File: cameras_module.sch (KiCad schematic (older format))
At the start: 22 parts, among them J3 WE_68715014522, U4 PCA9547BS

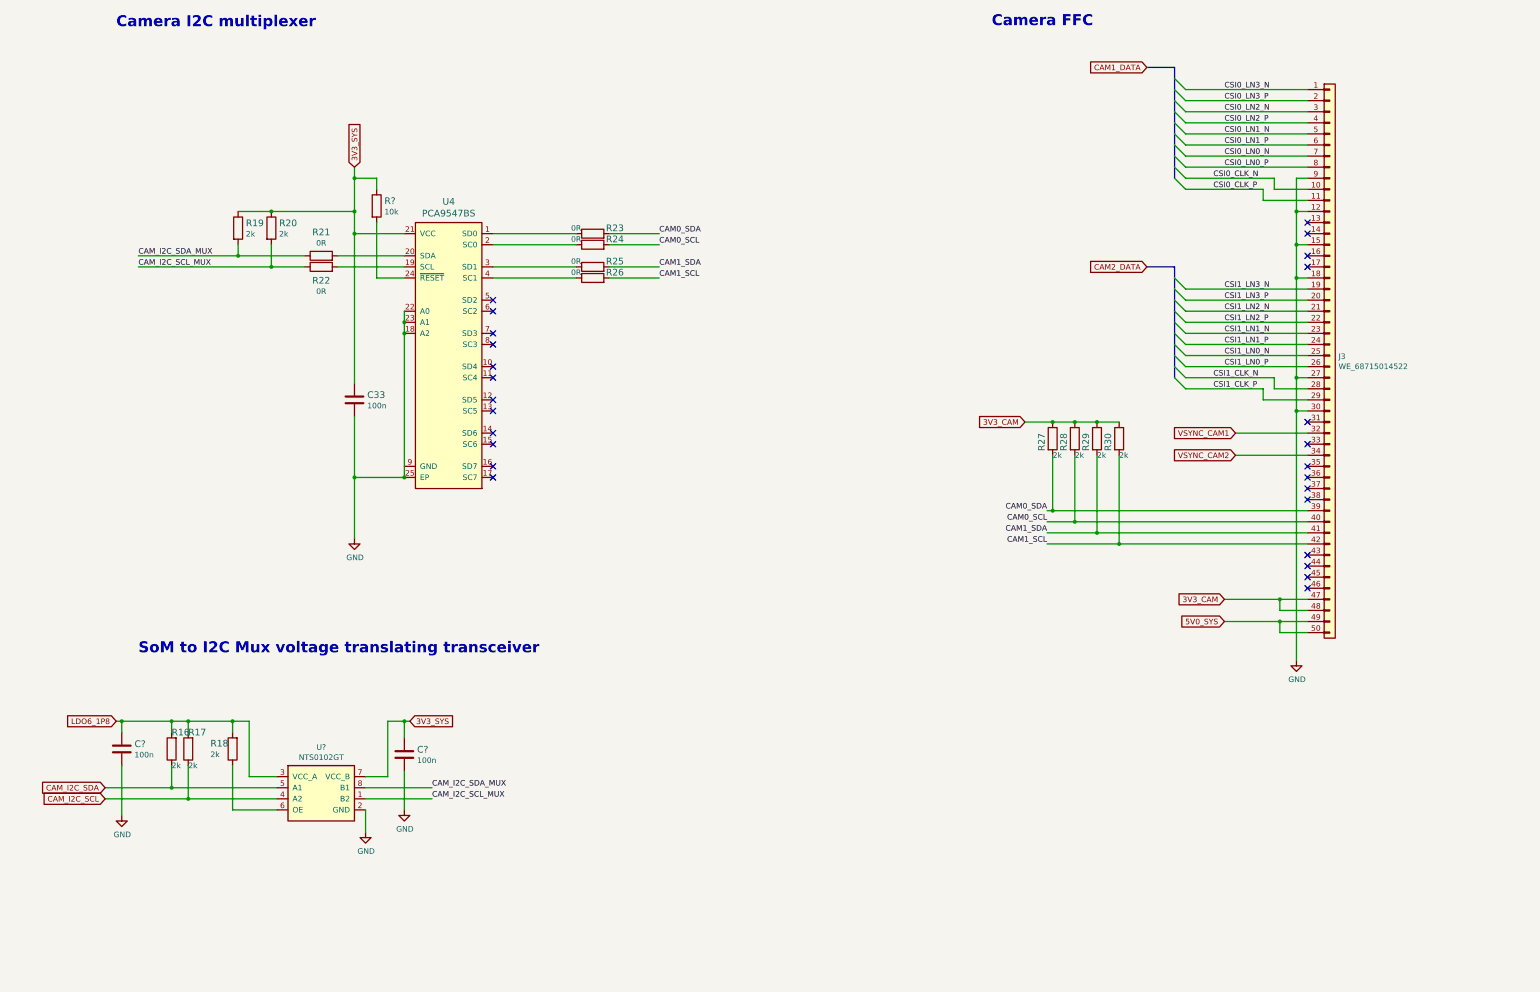
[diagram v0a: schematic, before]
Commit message: Started placing main components on PCB. Change of RT battery model and USB flash connector
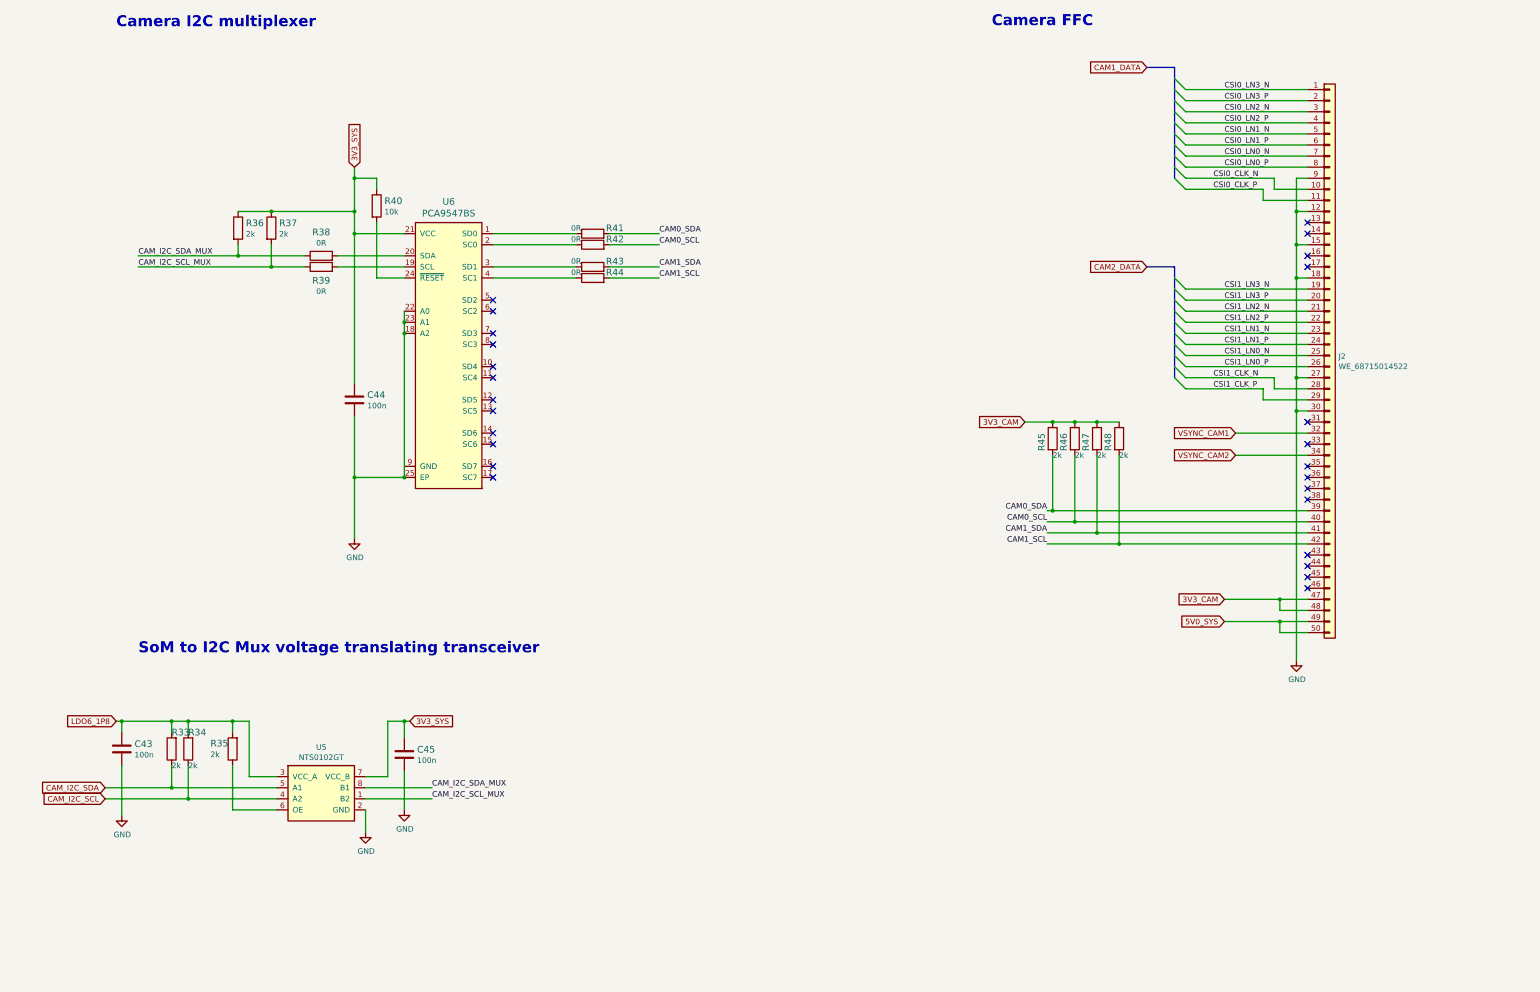
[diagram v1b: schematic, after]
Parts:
- gave numbers to parts that had none: 4
- renumbered C33 to C44, J3 to J2, R16 to R33, R17 to R34, R18 to R35, R19 to R36, R20 to R37, R21 to R38, R22 to R39, R23 to R41, R24 to R42, R25 to R43, R26 to R44, R27 to R45, R28 to R46, R29 to R47, R30 to R48, U4 to U6
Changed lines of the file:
@@
 Camera I2C multiplexer\n
 $Comp
-L sc606-baseboard:PCA9547BS U4
+L sc606-baseboard:PCA9547BS U6
 U 1 1 61E56C5B
 P 4950 4700
-F 0 "U4" H 4850 6089 60  0000 C CNN
+F 0 "U6" H 4850 6089 60  0000 C CNN
 F 1 "PCA9547BS" H 4850 5983 60  0000 C CNN
 F 2 "sc606-baseboard-footprints:VQFN-24" H 4700 3300 60  0001 C CNN
@@
 $EndComp
 $Comp
-L sc606-baseboard:C_100n_0402 C33
+L sc606-baseboard:C_100n_0402 C44
 U 1 1 61E589C6
 P 4000 5100
-F 0 "C33" H 4115 5145 60  0000 L CNN
+F 0 "C44" H 4115 5145 60  0000 L CNN
 F 1 "C_100n_0402" H 4000 4950 60  0001 C CNN
 F 2 "sc606-baseboard-footprints:0402-cap" H 4200 5300 60  0001 L CNN
@@
 	4000 3600 4000 4950
 $Comp
-L sc606-baseboard:GND #PWR042
+L sc606-baseboard:GND #PWR054
 U 1 1 61E5F2B7
 P 4000 6350
-F 0 "#PWR042" H 4000 6100 50  0001 C CNN
+F 0 "#PWR054" H 4000 6100 50  0001 C CNN
 F 1 "GND" H 4005 6177 50  0000 C CNN
 F 2 "" H 4000 6350 50  0001 C CNN
@@
 	3250 3900 2050 3900
 $Comp
-L sc606-baseboard:R_0R_0402 R21
+L sc606-baseboard:R_0R_0402 R38
 U 1 1 61E63E68
 P 3700 3800
-F 0 "R21" H 3700 4013 60  0000 C CNN
+F 0 "R38" H 3700 4013 60  0000 C CNN
 F 1 "R_0R_0402" H 3700 3650 60  0001 C CNN
 F 2 "sc606-baseboard-footprints:0402-res" H 3900 4000 60  0001 L CNN
@@
 	3850 3800 4450 3800
 $Comp
-L sc606-baseboard:R_0R_0402 R22
+L sc606-baseboard:R_0R_0402 R39
 U 1 1 61E641DF
 P 3700 3900
-F 0 "R22" H 3700 3777 60  0000 C CNN
+F 0 "R39" H 3700 3777 60  0000 C CNN
 F 1 "R_0R_0402" H 3700 3750 60  0001 C CNN
 F 2 "sc606-baseboard-footprints:0402-res" H 3900 4100 60  0001 L CNN
@@
 	2950 3400 3250 3400
 $Comp
-L sc606-baseboard:R_2k_0402 R19
+L sc606-baseboard:R_2k_0402 R36
 U 1 1 61E68958
 P 2950 3550
-F 0 "R19" V 2905 3620 60  0000 L CNN
+F 0 "R36" V 2905 3620 60  0000 L CNN
 F 1 "R_2k_0402" H 2950 3400 60  0001 C CNN
 F 2 "sc606-baseboard-footprints:0402-res" H 3150 3750 60  0001 L CNN
@@
 $EndComp
 $Comp
-L sc606-baseboard:R_2k_0402 R20
+L sc606-baseboard:R_2k_0402 R37
 U 1 1 61E68DEE
 P 3250 3550
-F 0 "R20" V 3205 3620 60  0000 L CNN
+F 0 "R37" V 3205 3620 60  0000 L CNN
 F 1 "R_2k_0402" H 3250 3400 60  0001 C CNN
 F 2 "sc606-baseboard-footprints:0402-res" H 3450 3750 60  0001 L CNN
@@
 	4450 4500 4450 5800
 $Comp
-L sc606-baseboard:R_0R_0402 R23
+L sc606-baseboard:R_0R_0402 R41
 U 1 1 61E6A5CA
 P 6150 3600
-F 0 "R23" H 6350 3650 60  0000 C CNN
+F 0 "R41" H 6350 3650 60  0000 C CNN
 F 1 "R_0R_0402" H 6150 3450 60  0001 C CNN
 F 2 "sc606-baseboard-footprints:0402-res" H 6350 3800 60  0001 L CNN
@@
 $EndComp
 $Comp
-L sc606-baseboard:R_0R_0402 R24
+L sc606-baseboard:R_0R_0402 R42
 U 1 1 61E6AAD1
 P 6150 3700
-F 0 "R24" H 6350 3750 60  0000 C CNN
+F 0 "R42" H 6350 3750 60  0000 C CNN
 F 1 "R_0R_0402" H 6150 3550 60  0001 C CNN
 F 2 "sc606-baseboard-footprints:0402-res" H 6350 3900 60  0001 L CNN
@@
 $EndComp
 $Comp
-L sc606-baseboard:R_0R_0402 R25
+L sc606-baseboard:R_0R_0402 R43
 U 1 1 61E6AE4A
 P 6150 3900
-F 0 "R25" H 6350 3950 60  0000 C CNN
+F 0 "R43" H 6350 3950 60  0000 C CNN
 F 1 "R_0R_0402" H 6150 3750 60  0001 C CNN
 F 2 "sc606-baseboard-footprints:0402-res" H 6350 4100 60  0001 L CNN
@@
 $EndComp
 $Comp
-L sc606-baseboard:R_0R_0402 R26
+L sc606-baseboard:R_0R_0402 R44
 U 1 1 61E6B0E9
 P 6150 4000
-F 0 "R26" H 6350 4050 60  0000 C CNN
+F 0 "R44" H 6350 4050 60  0000 C CNN
 F 1 "R_0R_0402" H 6150 3850 60  0001 C CNN
 F 2 "sc606-baseboard-footprints:0402-res" H 6350 4200 60  0001 L CNN
@@
 Camera FFC\n\n
 $Comp
-L sc606-baseboard:WE_68715014522 J3
+L sc606-baseboard:WE_68715014522 J2
 U 1 1 61E964B1
 P 12800 3900
-F 0 "J3" H 12880 3092 50  0000 L CNN
+F 0 "J2" H 12880 3092 50  0000 L CNN
 F 1 "WE_68715014522" H 12880 3001 50  0000 L CNN
 F 2 "sc606-baseboard-footprints:WE_68715014522" H 12600 350 50  0001 C CNN
@@
 	12600 6400 10900 6400
 $Comp
-L sc606-baseboard:R_2k_0402 R27
+L sc606-baseboard:R_2k_0402 R45
 U 1 1 61EAFCF7
 P 10300 5450
-F 0 "R27" H 10250 5350 60  0000 L CNN
+F 0 "R45" H 10250 5350 60  0000 L CNN
 F 1 "R_2k_0402" H 10300 5300 60  0001 C CNN
 F 2 "sc606-baseboard-footprints:0402-res" H 10500 5650 60  0001 L CNN
@@
 $EndComp
 $Comp
-L sc606-baseboard:R_2k_0402 R28
+L sc606-baseboard:R_2k_0402 R46
 U 1 1 61EB041B
 P 10500 5450
-F 0 "R28" H 10450 5350 60  0000 L CNN
+F 0 "R46" H 10450 5350 60  0000 L CNN
 F 1 "R_2k_0402" H 10500 5300 60  0001 C CNN
 F 2 "sc606-baseboard-footprints:0402-res" H 10700 5650 60  0001 L CNN
@@
 $EndComp
 $Comp
-L sc606-baseboard:R_2k_0402 R29
+L sc606-baseboard:R_2k_0402 R47
 U 1 1 61EB08C8
 P 10700 5450
-F 0 "R29" H 10650 5350 60  0000 L CNN
+F 0 "R47" H 10650 5350 60  0000 L CNN
 F 1 "R_2k_0402" H 10700 5300 60  0001 C CNN
 F 2 "sc606-baseboard-footprints:0402-res" H 10900 5650 60  0001 L CNN
@@
 $EndComp
 $Comp
-L sc606-baseboard:R_2k_0402 R30
+L sc606-baseboard:R_2k_0402 R48
 U 1 1 61EB0CC5
 P 10900 5450
-F 0 "R30" H 10850 5350 60  0000 L CNN
+F 0 "R48" H 10850 5350 60  0000 L CNN
 F 1 "R_2k_0402" H 10900 5300 60  0001 C CNN
 F 2 "sc606-baseboard-footprints:0402-res" H 11100 5650 60  0001 L CNN
@@
 CAM_I2C_SCL_MUX
 $Comp
-L sc606-baseboard:GND #PWR043
+L sc606-baseboard:GND #PWR055
 U 1 1 61EE63E6
 P 4100 9000
-F 0 "#PWR043" H 4100 8750 50  0001 C CNN
+F 0 "#PWR055" H 4100 8750 50  0001 C CNN
 F 1 "GND" H 4105 8827 50  0000 C CNN
 F 2 "" H 4100 9000 50  0001 C CNN
@@
 	2900 8800 3300 8800
 $Comp
-L sc606-baseboard:R_2k_0402 R18
+L sc606-baseboard:R_2k_0402 R35
 U 1 1 61FFF734
 P 2900 8250
-F 0 "R18" V 2950 8450 60  0000 R CNN
+F 0 "R35" V 2950 8450 60  0000 R CNN
 F 1 "R_2k_0402" H 2900 8100 60  0001 C CNN
 F 2 "sc606-baseboard-footprints:0402-res" H 3100 8450 60  0001 L CNN
@@
 $EndComp
 $Comp
-L sc606-baseboard:R_2k_0402 R16
+L sc606-baseboard:R_2k_0402 R33
 U 1 1 6200206C
 P 2350 8250
-F 0 "R16" V 2500 8250 60  0000 R CNN
+F 0 "R33" V 2500 8250 60  0000 R CNN
 F 1 "R_2k_0402" H 2350 8100 60  0001 C CNN
 F 2 "sc606-baseboard-footprints:0402-res" H 2550 8450 60  0001 L CNN
@@
 $EndComp
 $Comp
-L sc606-baseboard:R_2k_0402 R17
+L sc606-baseboard:R_2k_0402 R34
 U 1 1 62002978
 P 2500 8250
-F 0 "R17" V 2650 8250 60  0000 R CNN
+F 0 "R34" V 2650 8250 60  0000 R CNN
 F 1 "R_2k_0402" H 2500 8100 60  0001 C CNN
 F 2 "sc606-baseboard-footprints:0402-res" H 2700 8450 60  0001 L CNN
@@
 CAM_I2C_SCL
 $Comp
-L sc606-baseboard:GND #PWR044
+L sc606-baseboard:GND #PWR057
 U 1 1 6206201E
 P 12500 7450
-F 0 "#PWR044" H 12500 7200 50  0001 C CNN
+F 0 "#PWR057" H 12500 7200 50  0001 C CNN
 F 1 "GND" H 12505 7277 50  0000 C CNN
 F 2 "" H 12500 7450 50  0001 C CNN
@@
 	11400 3900 11150 3900
 $Comp
-L sc606-baseboard:NTS0102GT U?
+L sc606-baseboard:NTS0102GT U5
 U 1 1 62AE9D15
 P 3700 8750
-F 0 "U?" H 3700 9265 50  0000 C CNN
+F 0 "U5" H 3700 9265 50  0000 C CNN
 F 1 "NTS0102GT" H 3700 9174 50  0000 C CNN
 F 2 "sc606-baseboard-footprints:PSON50P100X195X50-8N" H 3600 9250 50  0001 C CNN
@@
 $EndComp
 $Comp
-L sc606-baseboard:R_10k_0402 R?
+L sc606-baseboard:R_10k_0402 R40
 U 1 1 62145419
 P 4200 3350
-F 0 "R?" V 4155 3420 60  0000 L CNN
+F 0 "R40" V 4155 3420 60  0000 L CNN
 F 1 "R_10k_0402" H 4200 3200 60  0001 C CNN
 F 2 "sc606-baseboard-footprints:0402-res" H 4400 3550 60  0001 L CNN
@@
 	4000 3100 4000 3400
 $Comp
-L sc606-baseboard:C_100n_0402 C?
+L sc606-baseboard:C_100n_0402 C45
 U 1 1 6214EFB5
 P 4450 8300
-F 0 "C?" H 4565 8345 60  0000 L CNN
+F 0 "C45" H 4565 8345 60  0000 L CNN
 F 1 "C_100n_0402" H 4450 8150 60  0001 C CNN
 F 2 "sc606-baseboard-footprints:0402-cap" H 4650 8500 60  0001 L CNN
@@
 $EndComp
 $Comp
-L sc606-baseboard:C_100n_0402 C?
+L sc606-baseboard:C_100n_0402 C43
 U 1 1 6214F58A
 P 1900 8250
-F 0 "C?" H 2015 8295 60  0000 L CNN
+F 0 "C43" H 2015 8295 60  0000 L CNN
 F 1 "C_100n_0402" H 1900 8100 60  0001 C CNN
 F 2 "sc606-baseboard-footprints:0402-cap" H 2100 8450 60  0001 L CNN
@@
 $EndComp
 $Comp
-L sc606-baseboard:GND #PWR?
+L sc606-baseboard:GND #PWR056
 U 1 1 6215CCFC
 P 4450 8800
-F 0 "#PWR?" H 4450 8550 50  0001 C CNN
+F 0 "#PWR056" H 4450 8550 50  0001 C CNN
 F 1 "GND" H 4455 8627 50  0000 C CNN
 F 2 "" H 4450 8800 50  0001 C CNN
@@
 $EndComp
 $Comp
-L sc606-baseboard:GND #PWR?
+L sc606-baseboard:GND #PWR053
 U 1 1 62161810
 P 1900 8850
-F 0 "#PWR?" H 1900 8600 50  0001 C CNN
+F 0 "#PWR053" H 1900 8600 50  0001 C CNN
 F 1 "GND" H 1905 8677 50  0000 C CNN
 F 2 "" H 1900 8850 50  0001 C CNN

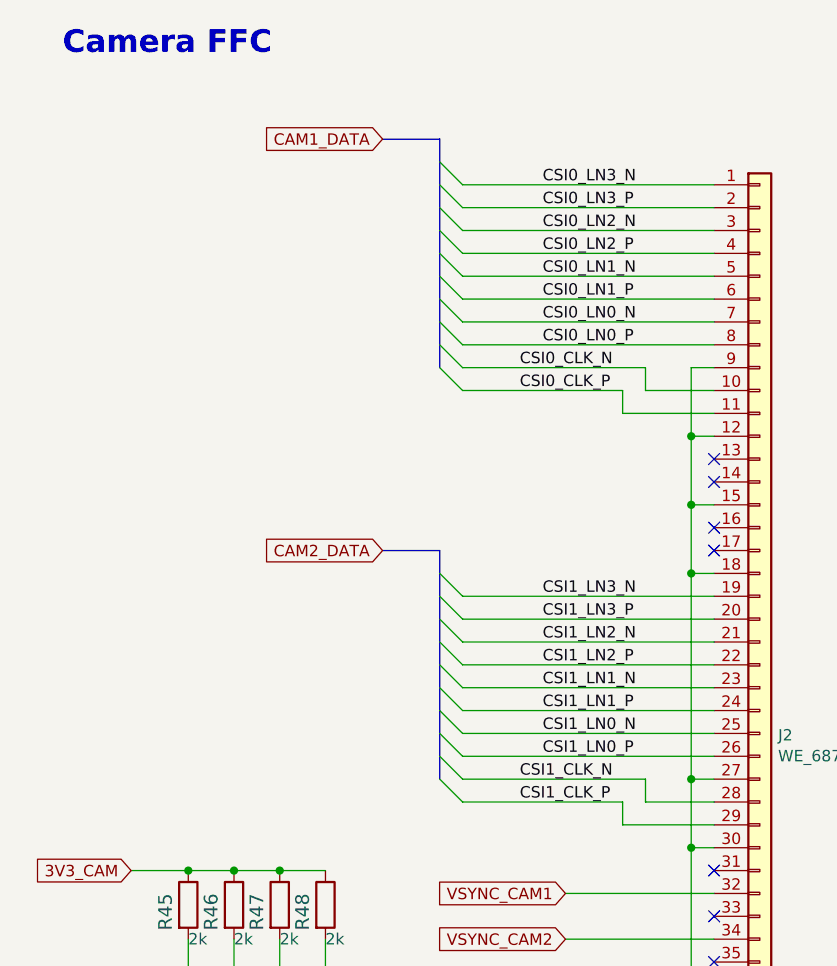
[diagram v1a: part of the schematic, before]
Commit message: Main components placed on board
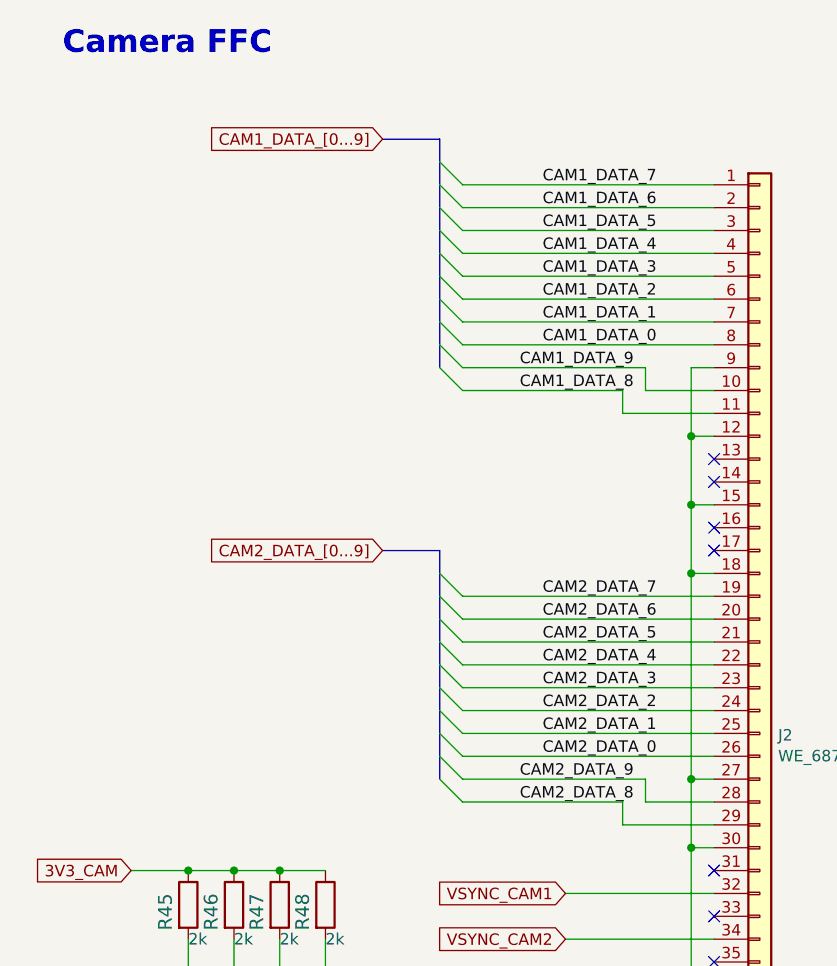
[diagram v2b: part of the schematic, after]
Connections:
- net CSI0_CLK_N renamed CAM1_DATA_9
- net CSI0_CLK_P renamed CAM1_DATA_8
- net CSI0_LN0_N renamed CAM1_DATA_1
- net CSI0_LN0_P renamed CAM1_DATA_0
- net CSI0_LN1_N renamed CAM1_DATA_3
- net CSI0_LN1_P renamed CAM1_DATA_2
- net CSI0_LN2_N renamed CAM1_DATA_5
- net CSI0_LN2_P renamed CAM1_DATA_4
- net CSI0_LN3_N renamed CAM1_DATA_7
- net CSI0_LN3_P renamed CAM1_DATA_6
- net CSI1_CLK_N renamed CAM2_DATA_9
- net CSI1_CLK_P renamed CAM2_DATA_8
- net CSI1_LN0_N renamed CAM2_DATA_1
- net CSI1_LN0_P renamed CAM2_DATA_0
- net CSI1_LN1_N renamed CAM2_DATA_3
- net CSI1_LN1_P renamed CAM2_DATA_2
- net CSI1_LN2_N renamed CAM2_DATA_5
- net CSI1_LN2_P renamed CAM2_DATA_4
- net CSI1_LN3_N renamed CAM2_DATA_7
- net CSI1_LN3_P renamed CAM2_DATA_6
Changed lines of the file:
@@
 	12200 3200 11500 3200
 Text Label 11850 2900 0    50   ~ 0
-CSI0_LN0_N
+CAM1_DATA_1
 Text Label 11850 3000 0    50   ~ 0
-CSI0_LN0_P
+CAM1_DATA_0
 Text Label 11850 2700 0    50   ~ 0
-CSI0_LN1_N
+CAM1_DATA_3
 Text Label 11850 2800 0    50   ~ 0
-CSI0_LN1_P
+CAM1_DATA_2
 Text Label 11850 2500 0    50   ~ 0
-CSI0_LN2_N
+CAM1_DATA_5
 Text Label 11850 2600 0    50   ~ 0
-CSI0_LN2_P
+CAM1_DATA_4
 Text Label 11850 2300 0    50   ~ 0
-CSI0_LN3_N
+CAM1_DATA_7
 Text Label 11850 2400 0    50   ~ 0
-CSI0_LN3_P
+CAM1_DATA_6
 Text Label 11750 3100 0    50   ~ 0
-CSI0_CLK_N
+CAM1_DATA_9
 Text Label 11750 3200 0    50   ~ 0
-CSI0_CLK_P
+CAM1_DATA_8
 Text GLabel 11150 2100 0    50   Input ~ 0
-CAM1_DATA
+CAM1_DATA_[0...9]
 Wire Bus Line
 	11400 2100 11150 2100
@@
 	12200 5000 11500 5000
 Text Label 11850 4700 0    50   ~ 0
-CSI1_LN0_N
+CAM2_DATA_1
 Text Label 11850 4800 0    50   ~ 0
-CSI1_LN0_P
+CAM2_DATA_0
 Text Label 11850 4500 0    50   ~ 0
-CSI1_LN1_N
+CAM2_DATA_3
 Text Label 11850 4600 0    50   ~ 0
-CSI1_LN1_P
+CAM2_DATA_2
 Text Label 11850 4300 0    50   ~ 0
-CSI1_LN2_N
+CAM2_DATA_5
 Text Label 11850 4400 0    50   ~ 0
-CSI1_LN2_P
+CAM2_DATA_4
 Text Label 11850 4100 0    50   ~ 0
-CSI1_LN3_N
+CAM2_DATA_7
 Text Label 11850 4200 0    50   ~ 0
-CSI1_LN3_P
+CAM2_DATA_6
 Text Label 11750 4900 0    50   ~ 0
-CSI1_CLK_N
+CAM2_DATA_9
 Text Label 11750 5000 0    50   ~ 0
-CSI1_CLK_P
+CAM2_DATA_8
 Text GLabel 11150 3900 0    50   Input ~ 0
-CAM2_DATA
+CAM2_DATA_[0...9]
 Wire Bus Line
 	11400 3900 11150 3900
